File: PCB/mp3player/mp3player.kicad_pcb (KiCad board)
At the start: 2 copper layers, 60 x 85.5 mm, 70 parts, among them J1 AudioJack3, J2 Battery, J3 USB_C, J4 Micro_SD_Card, J5 TFT SPI, SW1 Play, SW10 Power_sw, SW11 Next, SW12 Prev, SW2 Trk Prev, SW3 Trk Next, SW4 Mode Prev, SW5 Mode Next, SW6 Eq, SW7 Power, SW8 RESET, SW9 BOOT, U1 ESP32-S3-WROOM-1, U2 ES8388, U3 AP2112K-3.3, U4 MCP73831-2-OT, U5 USBLC6-2SC6

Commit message: cont
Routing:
- net GND: track 92.6 -> 100.1 mm, vias 4 -> 9
- net +3V3: track 203.9 -> 208.7 mm, vias 13 -> 14
- net (no net): track 0.00 -> 2.12 mm, vias 0 -> 2
- net /LOUT1: track 34.1 -> 35.6 mm

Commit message: cont
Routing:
- net AU_GND: track 119.6 -> 121.7 mm
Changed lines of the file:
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@@
 	)
 	(segment
+		(start 237.400001 114.199999)
+		(end 237.400001 114.549999)
+		(width 0.2)
+		(layer "F.Cu")
+		(net "VDD_CODEC")
+	)
+	(segment
+		(start 239.2 112.75)
+		(end 238.85 112.75)
+		(width 0.2)
+		(layer "F.Cu")
+		(net "VDD_CODEC")
+	)
+	(segment
 		(start 241.5 114.75)
 		(end 243 113.25)
@@
 	)
 	(segment
-		(start 243.75 114)
-		(end 243.75 112.5)
+		(start 238.85 112.75)
+		(end 237.400001 114.199999)
 		(width 0.2)
 		(layer "F.Cu")
@@
 	)
 	(segment
-		(start 239.2 112.75)
-		(end 237.400001 114.549999)
+		(start 243.75 114)
+		(end 243.75 112.5)
 		(width 0.2)
 		(layer "F.Cu")
@@
 	)
 	(segment
-		(start 239.225 114.75)
-		(end 239.225 114.234281)
-		(width 0.2)
-		(layer "F.Cu")
-		(net "AU_GND")
-	)
-	(segment
 		(start 243.75 119)
 		(end 243.75 118.44)
@@
 	)
 	(segment
+		(start 239.225 114.337032)
+		(end 238.697063 113.809095)
+		(width 0.2)
+		(layer "F.Cu")
+		(net "AU_GND")
+	)
+	(segment
 		(start 232 118.5)
 		(end 231.217437 117.717437)
@@
 	)
 	(segment
-		(start 239.225 114.234281)
-		(end 239.65 113.809281)
+		(start 240.75 113.451922)
+		(end 241.075983 113.777905)
 		(width 0.2)
 		(layer "F.Cu")
@@
 	)
 	(segment
-		(start 240.75 113.709281)
-		(end 240.85 113.809281)
+		(start 240.75 112.75)
+		(end 240.75 113.451922)
 		(width 0.2)
 		(layer "F.Cu")
@@
 	)
 	(segment
+		(start 239.225 114.75)
+		(end 239.225 114.337032)
+		(width 0.2)
+		(layer "F.Cu")
+		(net "AU_GND")
+	)
+	(segment
 		(start 186.425 85)
 		(end 186.425 86.5)
@@
 	)
 	(segment
-		(start 240.75 112.75)
-		(end 240.75 113.709281)
-		(width 0.2)
-		(layer "F.Cu")
-		(net "AU_GND")
-	)
-	(segment
 		(start 192.5 80.197056)
 		(end 192.5 79.75)
@@
 	)
 	(via
-		(at 239.65 113.809281)
+		(at 192.5 79.75)
 		(size 0.6)
 		(drill 0.3)
@@
 	)
 	(via
-		(at 192.5 79.75)
+		(at 235.944048 116.329629)
 		(size 0.6)
 		(drill 0.3)
@@
 	)
 	(via
-		(at 235.944048 116.329629)
+		(at 243.56 118.25)
 		(size 0.6)
 		(drill 0.3)
@@
 	)
 	(via
-		(at 243.56 118.25)
+		(at 235.7 114.745679)
 		(size 0.6)
 		(drill 0.3)
@@
 	)
 	(via
-		(at 235.7 114.745679)
+		(at 236.9 113.75)
 		(size 0.6)
 		(drill 0.3)
@@
 	)
 	(via
-		(at 236.9 113.75)
+		(at 225.298528 97.8)
 		(size 0.6)
 		(drill 0.3)
@@
 	)
 	(via
-		(at 240.85 113.809281)
+		(at 243.598812 114.95)
 		(size 0.6)
 		(drill 0.3)
@@
 	)
 	(via
-		(at 225.298528 97.8)
+		(at 238.697063 113.809095)
 		(size 0.6)
 		(drill 0.3)
@@
 	)
 	(via
-		(at 243.598812 114.95)
+		(at 241.075983 113.777905)
 		(size 0.6)
 		(drill 0.3)
@@
 	)
 	(segment
+		(start 237.95 113.809281)
+		(end 239.9 113.809281)
+		(width 0.2)
+		(layer "B.Cu")
+		(net "AU_GND")
+	)
+	(segment
 		(start 243.56 118.25)
 		(end 243.598812 118.211188)
@@
 	(segment
 		(start 240.25 99)
-		(end 240.25 115.5)
+		(end 240.25 111.25)
+		(width 0.2)
+		(layer "F.Cu")
+		(net "/12C_SDA")
+	)
+	(segment
+		(start 240 111.5)
+		(end 240 115.75)
 		(width 0.2)
 		(layer "F.Cu")
@@
 	)
 	(segment
-		(start 240.25 115.5)
+		(start 240.25 111.25)
+		(end 240 111.5)
+		(width 0.2)
+		(layer "F.Cu")
+		(net "/12C_SDA")
+	)
+	(segment
+		(start 240 115.75)
 		(end 239 116.75)
 		(width 0.2)
@@
 	)
 	(segment
-		(start 234.75 110.75)
-		(end 234.55 110.55)
-		(width 0.2)
-		(layer "F.Cu")
-		(net "/12C_SCL")
-	)
-	(segment
-		(start 237.75 116.409281)
-		(end 237.75 115.75)
-		(width 0.2)
-		(layer "F.Cu")
-		(net "/12C_SCL")
-	)
-	(segment
 		(start 237.659281 116.5)
 		(end 237.75 116.409281)
@@
 	)
 	(segment
-		(start 237.5 115.5)
-		(end 235 115.5)
+		(start 234.55 115.05)
+		(end 234.55 109.45)
 		(width 0.2)
 		(layer "F.Cu")
@@
 	)
 	(segment
-		(start 234.75 109.25)
-		(end 234.75 104)
+		(start 234.55 109.45)
+		(end 234.75 109.25)
 		(width 0.2)
 		(layer "F.Cu")
@@
 	)
 	(segment
-		(start 235 115.5)
-		(end 234.75 115.25)
+		(start 237.75 116.409281)
+		(end 237.75 115.75)
 		(width 0.2)
 		(layer "F.Cu")
@@
 	)
 	(segment
-		(start 234.55 110.55)
-		(end 234.55 109.45)
+		(start 235 115.5)
+		(end 234.55 115.05)
 		(width 0.2)
 		(layer "F.Cu")
@@
 	)
 	(segment
-		(start 234.75 115.25)
-		(end 234.75 110.75)
+		(start 234.75 109.25)
+		(end 234.75 104)
 		(width 0.2)
 		(layer "F.Cu")
@@
 	)
 	(segment
-		(start 234.55 109.45)
-		(end 234.75 109.25)
+		(start 237.5 115.5)
+		(end 235 115.5)
 		(width 0.2)
 		(layer "F.Cu")

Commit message: working on drc
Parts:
- moved SW10 0.25 mm to (190.1, 94.0)
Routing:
- net GND: track 100.1 -> 126.0 mm, vias 9 -> 20
- net +3V3: track 208.7 -> 231.1 mm, vias 14 -> 16
- net AU_GND: track 121.7 -> 134.1 mm, vias 13 -> 16
- net /IO0: track 40.8 -> 41.2 mm, vias 1 -> 3

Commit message: No DRC errors, fuck warnings
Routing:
- net GND: track 126.0 -> 125.8 mm, vias 20 -> 22
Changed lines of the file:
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@@
 	)
 	(via
+		(at 227.25 86)
+		(size 1)
+		(drill 0.7)
+		(layers "F.Cu" "B.Cu")
+		(net "GND")
+	)
+	(via
 		(at 243.25 123.5)
 		(size 0.6)
@@
 	)
 	(via
+		(at 237 84)
+		(size 1)
+		(drill 0.7)
+		(layers "F.Cu" "B.Cu")
+		(net "GND")
+	)
+	(via
 		(at 235.5 105)
 		(size 0.6)
@@
 	)
 	(segment
-		(start 242.525 91)
-		(end 242.525 85.5)
+		(start 200.8 93.5)
+		(end 199.8 94.5)
 		(width 0.2)
 		(layer "B.Cu")
@@
 	)
 	(segment
-		(start 200.8 93.5)
-		(end 199.8 94.5)
-		(width 0.2)
+		(start 226.13 84.88)
+		(end 227.25 86)
+		(width 1)
 		(layer "B.Cu")
 		(net "GND")
@@
 	)
 	(segment
-		(start 242.525 85.5)
-		(end 241.75 84.725)
-		(width 0.2)
-		(layer "B.Cu")
-		(net "GND")
-	)
-	(segment
 		(start 199.8 94.5)
 		(end 198.25 94.5)
@@
 	)
 	(segment
+		(start 221.4 84.88)
+		(end 226.13 84.88)
+		(width 1)
+		(layer "B.Cu")
+		(net "GND")
+	)
+	(segment
 		(start 219 92.25)
 		(end 218.010003 93.239997)
@@
 	)
 	(segment
-		(start 242.525 118.75)
-		(end 242.476001 118.701001)
-		(width 0.2)
-		(layer "B.Cu")
-		(net "/VMID")
-	)
-	(segment
 		(start 241.75 118.75)
 		(end 242.56 117.94)
@@
 	)
 	(zone
+		(layers "F.Cu" "B.Cu")
+		(hatch full 0.5)
+		(connect_pads
+			(clearance 0)
+		)
+		(min_thickness 0.25)
+		(keepout
+			(tracks allowed)
+			(vias allowed)
+			(pads allowed)
+			(copperpour not_allowed)
+			(footprints allowed)
+		)
+		(placement
+			(enabled no)
+			(sheetname "/")
+		)
+		(fill
+			(thermal_gap 0.5)
+			(thermal_bridge_width 0.5)
+			(island_removal_mode 0)
+		)
+		(polygon
+			(pts
+				(xy 216 91) (xy 219.5 91) (xy 219.5 93.25) (xy 216 93.25)
+			)
+		)
+	)
+	(zone
 		(net "GND")
 		(layers "F.Cu" "B.Cu")
@@
 			)
 		)
+	)
+	(zone
+		(layer "B.Cu")
+		(hatch full 0.5)
+		(connect_pads
+			(clearance 0)
+		)
+		(min_thickness 0.25)
+		(keepout
+			(tracks allowed)
+			(vias allowed)
+			(pads allowed)
+			(copperpour not_allowed)
+			(footprints allowed)
+		)
+		(placement
+			(enabled no)
+			(sheetname "/")
+		)
+		(fill
+			(thermal_gap 0.5)
+			(thermal_bridge_width 0.5)
+			(island_removal_mode 0)
+		)
+		(polygon
+			(pts
+				(xy 215 83.75) (xy 228.25 83.75) (xy 228.25 88.25) (xy 224.25 88.25) (xy 221.5 85.5) (xy 217.5 86)
+				(xy 214 85.75)
+			)
+		)

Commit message: drc is CLEAN isudhfguoishgf
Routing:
- net (no net): track 2.12 -> 0.00 mm, vias 2 -> 0
- net /SD_CMD: track 63.5 -> 63.3 mm, vias 6 -> 5
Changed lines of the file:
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@@
 		(tags "capacitor")
 		(property "Reference" "C1"
-			(at 0 -1.68 0)
+			(at 0 1.75 0)
 			(layer "F.SilkS")
 			(effects
@@
 		(tags "capacitor")
 		(property "Reference" "C4"
-			(at 0 -1.43 0)
+			(at 0.025 -1.25 0)
 			(layer "F.SilkS")
 			(effects
@@
 		(tags "capacitor")
 		(property "Reference" "C8"
-			(at 2.7 -0.25 90)
+			(at -0.05 1.5 90)
 			(layer "F.SilkS")
 			(effects
@@
 		(tags "SOT TO_SOT_SMD")
 		(property "Reference" "U4"
-			(at 0 -2.4 0)
+			(at 0 2.45 0)
 			(layer "F.SilkS")
 			(effects
@@
 		(tags "capacitor")
 		(property "Reference" "C6"
-			(at 1.975 1 90)
+			(at -0.025 1.25 90)
 			(layer "F.SilkS")
 			(effects
@@
 		(tags "resistor")
 		(property "Reference" "R17"
-			(at 0 -1.43 90)
+			(at 0 -1.25 90)
 			(layer "F.SilkS")
 			(effects
@@
 		(tags "resistor")
 		(property "Reference" "R5"
-			(at 0 -1.43 0)
+			(at 0 1.5 0)
 			(layer "F.SilkS")
 			(effects
@@
 		(tags "resistor")
 		(property "Reference" "R7"
-			(at 0 -1.43 90)
+			(at 0 1.25 90)
 			(layer "F.SilkS")
 			(effects
@@
 		(tags "SOT TO_SOT_SMD")
 		(property "Reference" "U3"
-			(at 0 -2.4 0)
+			(at 0 2.25 0)
 			(layer "F.SilkS")
 			(effects
@@
 		)
 		(property "Value" "AP2112K-3.3"
-			(at 0 2.4 0)
+			(at 0.25 0 0)
 			(layer "F.Fab")
+			(hide yes)
 			(effects
 				(font
@@
 		(tags "capacitor")
 		(property "Reference" "C20"
-			(at 0 -1.68 0)
+			(at 3.25 0 0)
 			(layer "F.SilkS")
 			(effects
@@
 		(tags "resistor")
 		(property "Reference" "R24"
-			(at 0 1.43 90)
+			(at 0 -1.5 90)
 			(layer "B.SilkS")
 			(effects
@@
 		(tags "Through hole angled socket strip THT 1x02 2.00mm single row")
 		(property "Reference" "J2"
-			(at -3.31 2.5 0)
+			(at 1.5 -1 0)
 			(layer "B.SilkS")
 			(effects
@@
 		(tags "resistor")
 		(property "Reference" "R20"
-			(at 0 1.43 0)
+			(at 0 1.5 0)
 			(layer "B.SilkS")
 			(effects
@@
 		(tags "QFN NoLead")
 		(property "Reference" "U2"
-			(at 0 3.3 0)
+			(at 0 -3.309281 0)
 			(layer "B.SilkS")
 			(effects
@@
 		(tags "resistor")
 		(property "Reference" "R22"
-			(at 0 1.43 90)
+			(at 0 1.5 90)
 			(layer "B.SilkS")
 			(effects
@@
 		(tags "resistor")
 		(property "Reference" "R15"
-			(at 0 1.43 90)
+			(at 3 0 90)
 			(layer "B.SilkS")
 			(effects
@@
 		(tags "resistor")
 		(property "Reference" "R12"
-			(at 0 1.43 0)
+			(at 2.5 0 0)
 			(layer "B.SilkS")
 			(effects
 				(font
-					(size 1 1)
-					(thickness 0.15)
+					(size 0.7 0.7)
+					(thickness 0.12)
+					(bold yes)
 				)
 				(justify mirror)
@@
 		(tags "capacitor")
 		(property "Reference" "C14"
-			(at 0 1.43 0)
+			(at 0 -1.5 0)
 			(layer "B.SilkS")
 			(effects
@@
 		(tags "capacitor")
 		(property "Reference" "C7"
-			(at 0 1.43 90)
+			(at 0 -1.25 90)
 			(layer "B.SilkS")
 			(effects
@@
 		(tags "resistor")
 		(property "Reference" "R14"
-			(at 0 1.43 90)
+			(at -3 0 90)
 			(layer "B.SilkS")
 			(effects
@@
 		(tags "resistor")
 		(property "Reference" "R21"
-			(at 0 1.43 0)
+			(at 0 -1.5 0)
 			(layer "B.SilkS")
 			(effects
@@
 		(tags "resistor")
 		(property "Reference" "R4"
-			(at 0 1.43 90)
+			(at -2.425 0 90)
 			(layer "B.SilkS")
 			(effects
@@
 			(at 0 -1.43 90)
 			(layer "B.Fab")
+			(hide yes)
 			(effects
 				(font
@@
 		)
 		(fp_text user "${REFERENCE}"
-			(at 0 0 90)
+			(at -1.925 -0.5 90)
 			(layer "B.Fab")
 			(effects
@@
 		(tags "capacitor")
 		(property "Reference" "C15"
-			(at 0 1.68 0)
+			(at 3.25 0 0)
 			(layer "B.SilkS")
 			(effects
@@
 		(tags "resistor")
 		(property "Reference" "R23"
-			(at 0 1.43 0)
+			(at 0 -1.5 0)
 			(layer "B.SilkS")
 			(effects
@@
 		(tags "resistor")
 		(property "Reference" "R10"
-			(at 0 1.43 0)
+			(at 2.5 0 180)
 			(layer "B.SilkS")
 			(effects
 				(font
-					(size 1 1)
-					(thickness 0.15)
+					(size 0.7 0.7)
+					(thickness 0.12)
+					(bold yes)
 				)
 				(justify mirror)
@@
 		(tags "resistor")
 		(property "Reference" "R8"
-			(at 0 1.43 0)
+			(at 2.75 -0.75 0)
 			(layer "B.SilkS")
 			(effects
@@
 		(tags "resistor")
 		(property "Reference" "R9"
-			(at 0 1.43 0)
+			(at 2.5 0 0)
 			(layer "B.SilkS")
 			(effects
@@
 		(tags "capacitor")
 		(property "Reference" "C2"
-			(at 0 1.43 90)
+			(at 0 1.75 180)
 			(layer "B.SilkS")
 			(effects
@@
 		(tags "resistor")
 		(property "Reference" "R3"
-			(at 0 1.43 90)
+			(at -2.425 0 90)
 			(layer "B.SilkS")
 			(effects
@@
 		)
 		(property "Value" "5.1"
-			(at 0 -1.43 90)
+			(at 0 -1.5 90)
 			(layer "B.Fab")
+			(hide yes)
 			(effects
 				(font
@@
 		)
 		(fp_text user "${REFERENCE}"
-			(at 0 0 90)
+			(at -1.925 0.5 90)
 			(layer "B.Fab")
 			(effects
@@
 		(tags "resistor")
 		(property "Reference" "R11"
-			(at 0 1.43 0)
+			(at 2.5 0 0)
 			(layer "B.SilkS")
 			(effects
 				(font
-					(size 1 1)
-					(thickness 0.15)
+					(size 0.7 0.7)
+					(thickness 0.12)
+					(bold yes)
 				)
 				(justify mirror)
@@
 		(tags "capacitor electrolytic")
 		(property "Reference" "C9"
-			(at 0 4.35 0)
+			(at -5.203246 0 90)
 			(layer "B.SilkS")
 			(effects
@@
 		(tags "capacitor electrolytic")
 		(property "Reference" "C10"
-			(at 0 4.35 0)
+			(at -5.203246 0 90)
 			(layer "B.SilkS")
 			(effects
@@
 		(tags "resistor")
 		(property "Reference" "R13"
-			(at 0 1.43 0)
+			(at 2.5 0 0)
 			(layer "B.SilkS")
 			(effects
 				(font
-					(size 1 1)
-					(thickness 0.15)
+					(size 0.7 0.7)
+					(thickness 0.12)
+					(bold yes)
 				)
 				(justify mirror)
@@
 		)
 	)
+	(gr_line
+		(start 235.4 117.75)
+		(end 235.9 117.25)
+		(stroke
+			(width 0.1)
+			(type solid)
+		)
+		(layer "B.SilkS")
+	)
 	(gr_rect
 		(start 185 76.5)
@@
 		)
 	)
-	(via
-		(at 188.25 92.5)
-		(size 0.6)
-		(drill 0.3)
-		(layers "F.Cu" "B.Cu")
-		(net "")
-	)
-	(via
-		(at 189.75 91)
-		(size 0.6)
-		(drill 0.3)
-		(layers "F.Cu" "B.Cu")
-		(net "")
-	)
-	(segment
-		(start 189.75 91)
-		(end 188.25 92.5)
-		(width 0.2)
-		(layer "B.Cu")
-		(net "")
-	)
 	(segment
 		(start 243.75 89.5)
@@
 	)
 	(segment
-		(start 188.4225 105.5)
-		(end 189.3725 105.5)
-		(width 0.2)
-		(layer "F.Cu")
-		(net "/SD_CMD")
-	)
-	(segment
-		(start 222.15 89.4)
-		(end 222.15 89.748529)
+		(start 225.080911 91.330912)
+		(end 225.080911 92.029674)
 		(width 0.2)
 		(layer "F.Cu")
@@
 	)
 	(segment
-		(start 225.25 91.5)
-		(end 225.25 91.658881)
+		(start 188.4225 105.5)
+		(end 189.3725 105.5)
 		(width 0.2)
 		(layer "F.Cu")
@@
 	)
 	(segment
-		(start 225.25 91.658881)
-		(end 224.399148 92.509733)
+		(start 222.15 89.4)
+		(end 222.15 89.748529)
 		(width 0.2)
 		(layer "F.Cu")
@@
 	)
 	(segment
-		(start 224.5 92.610585)
-		(end 224.399148 92.509733)
+		(start 223.85 90.1)
+		(end 225.080911 91.330912)
 		(width 0.2)
 		(layer "F.Cu")
@@
 	)
 	(segment
+		(start 225.080911 92.029674)
+		(end 224.5 92.610585)
+		(width 0.2)
+		(layer "F.Cu")
+		(net "/SD_CMD")
+	)
+	(segment
 		(start 216.2835 88.679087)
 		(end 209.189541 88.679087)
@@
 	)
 	(segment
-		(start 223.85 90.1)
-		(end 225.25 91.5)
-		(width 0.2)
-		(layer "F.Cu")
-		(net "/SD_CMD")
-	)
-	(segment
 		(start 218.074266 88.079087)
 		(end 220.829087 88.079087)
@@
 		(size 0.6)
 		(drill 0.3)
-		(layers "F.Cu" "B.Cu")
-		(net "/SD_CMD")
-	)
-	(via
-		(at 224.399148 92.509733)
-		(size 0.6)
-		(drill 0.3)

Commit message: started on silkscreen design
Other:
- board text added: "modeck mk1"

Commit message: board design
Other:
- board text added: "github.com/Noxel43/modeck-mk1"

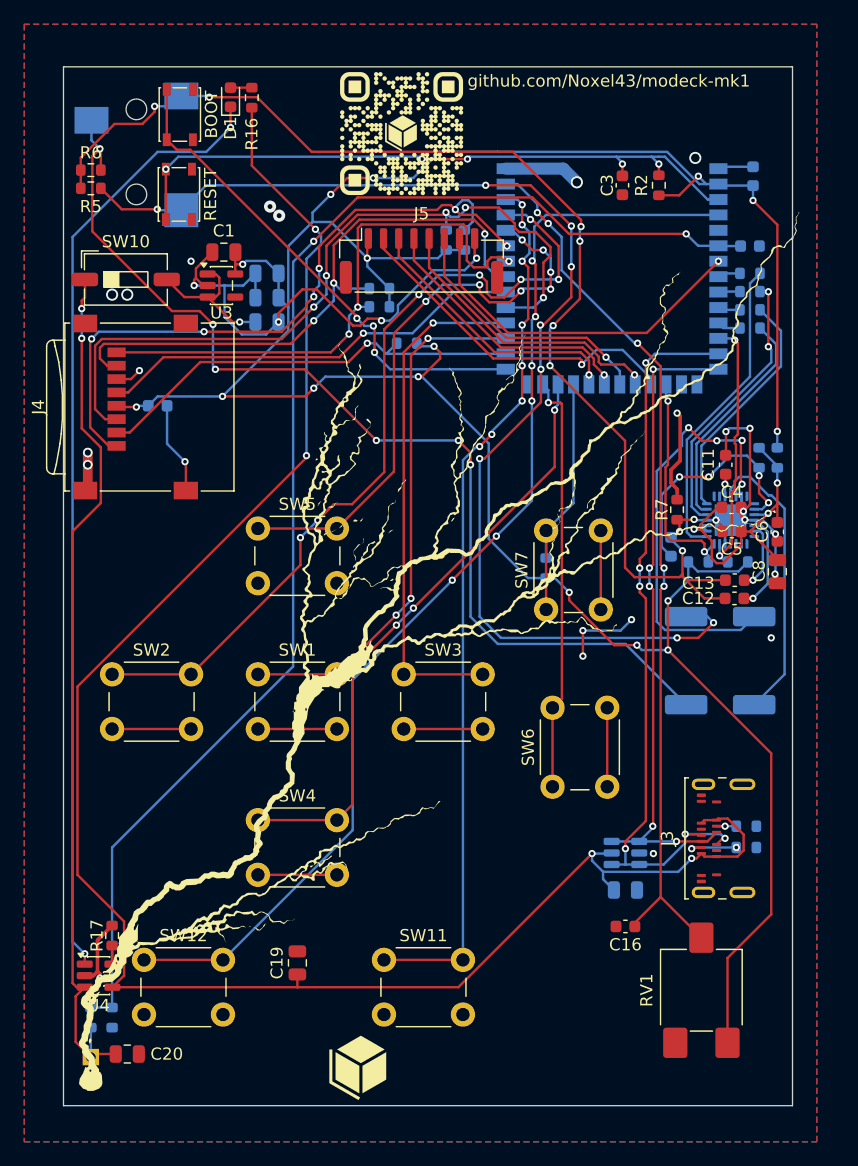
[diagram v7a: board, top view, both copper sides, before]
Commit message: added m2 mounting holes
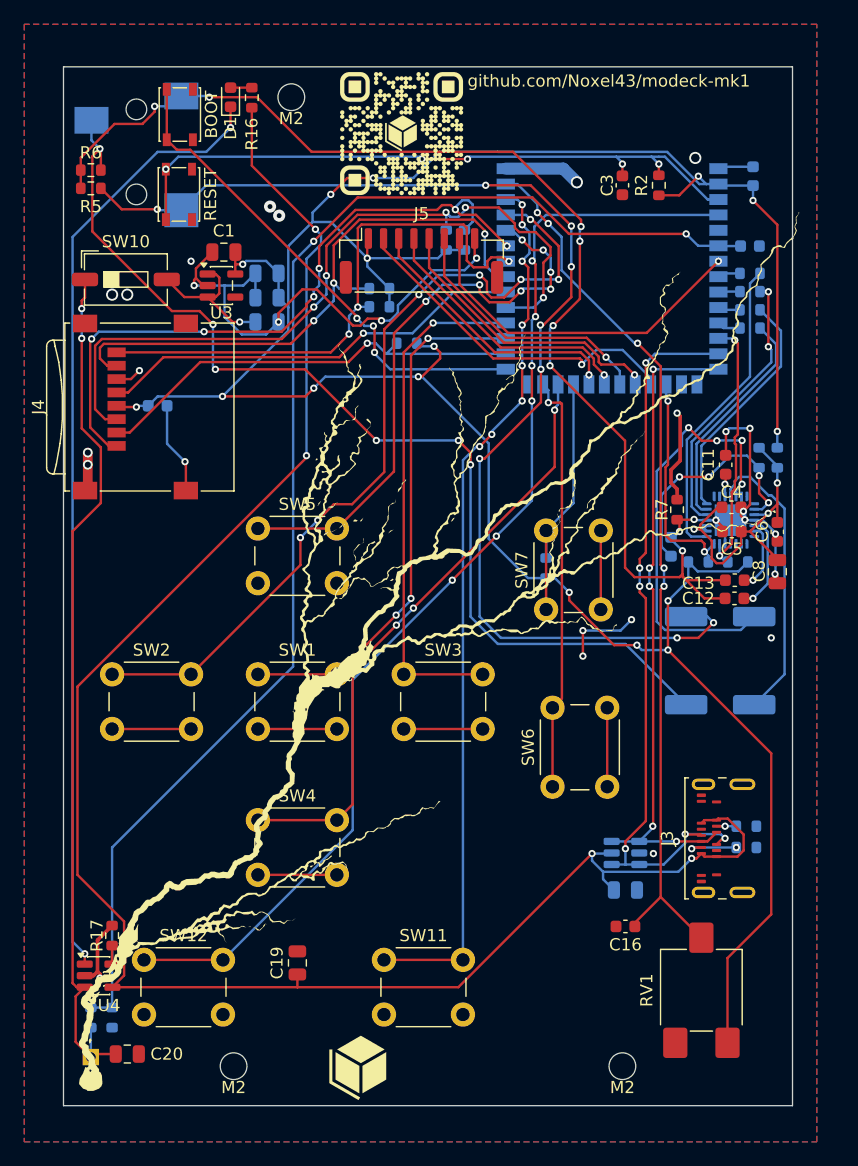
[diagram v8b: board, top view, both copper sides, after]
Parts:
- added M2: MountingHole_2.2mm_M2, MountingHole:MountingHole_2.2mm_M2, F.Cu at (203.8, 79.0)
- added M2: MountingHole_2.2mm_M2, MountingHole:MountingHole_2.2mm_M2, F.Cu at (231.0, 158.8)
- added M2: MountingHole_2.2mm_M2, MountingHole:MountingHole_2.2mm_M2, F.Cu at (199.0, 158.8)
